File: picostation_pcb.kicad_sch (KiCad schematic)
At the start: 13 parts, among them J1 Conn_01x06_Female, J2 Conn_01x20_Female, J3 PICO, J4 Conn_02x10_Female, U1 LM78M05_TO252

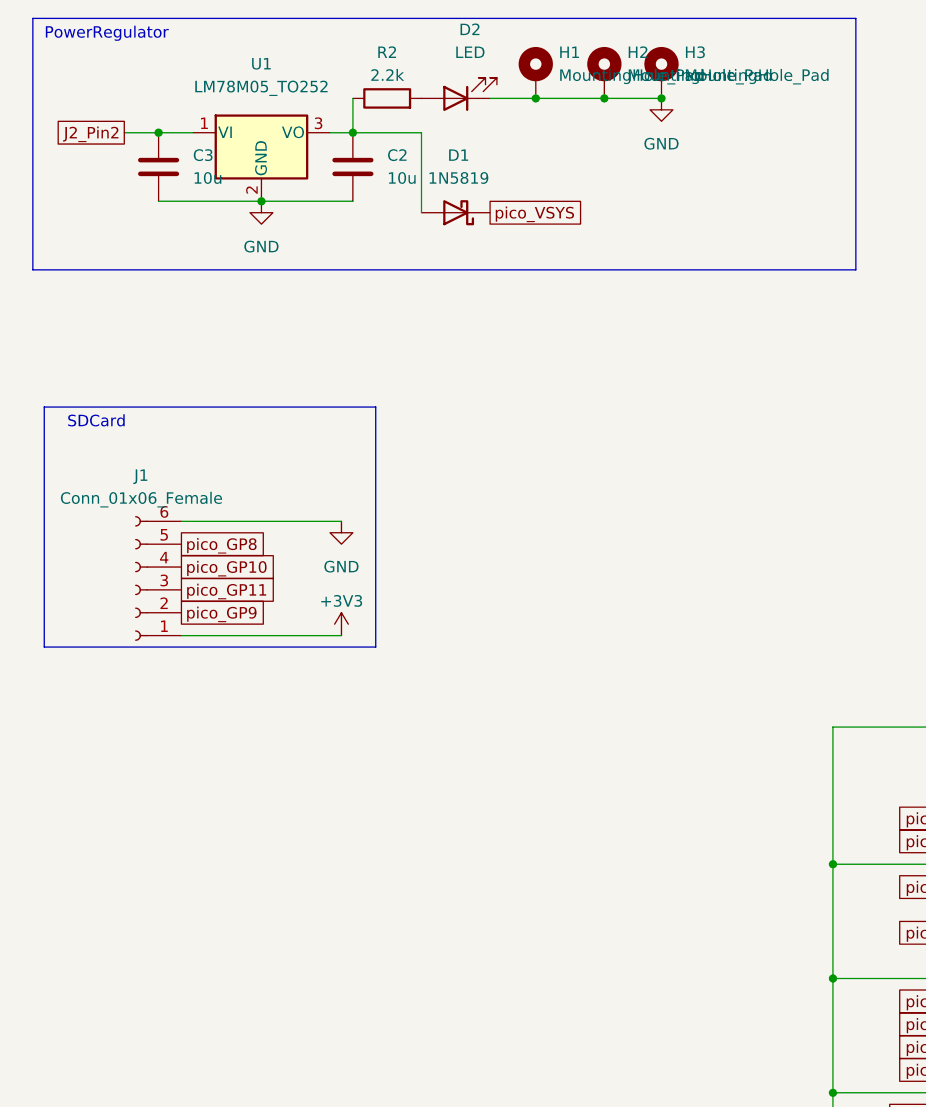
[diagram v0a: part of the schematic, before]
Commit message: Added SDCard directly to pcb, added through holes for breakout board
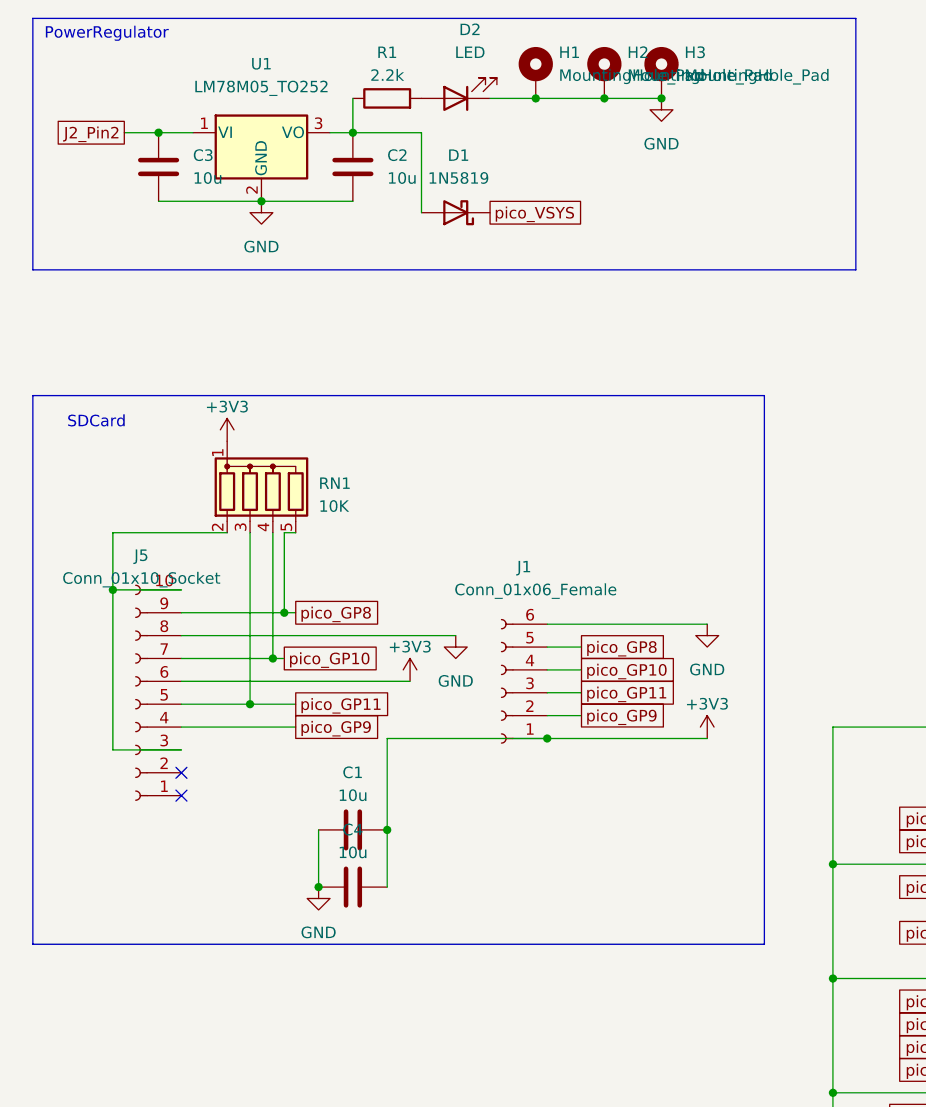
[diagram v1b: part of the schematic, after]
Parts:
- added C1, C4: 10u, Capacitor_SMD:C_0805_2012Metric_Pad1.18x1.45mm_HandSolder, symbol Device:C
- added J5: Conn_01x10_Socket, symbol Connector:Conn_01x10_Socket
- added RN1: 10K, Resistor_THT:R_Array_SIP5, symbol Device:R_Network04
- renumbered R2 to R1
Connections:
- net +3V3: now also C1.2, C4.2, J5.6 (Pin_6), RN1.1 (common)
- net GND: now also C1.1, C4.1, J5.8 (Pin_8)
- net pico_GP10: now also J5.7 (Pin_7), RN1.4 (R3)
- net pico_GP11: now also J5.5 (Pin_5), RN1.3 (R2)
- net pico_GP8: now also J5.9 (Pin_9), RN1.5 (R4)
- net pico_GP9: now also J5.4 (Pin_4)
- new net: J5.10 (Pin_10), J5.3 (Pin_3), RN1.2 (R1)
- no-connect marks 12 -> 14
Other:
- moved on the sheet: J1
